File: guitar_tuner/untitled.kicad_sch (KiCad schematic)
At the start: 1 part, among them J1 USB_B_Micro

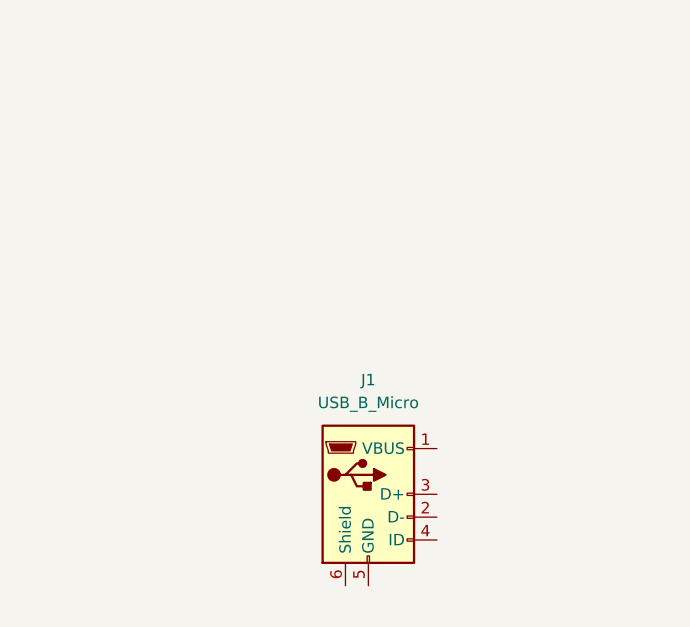
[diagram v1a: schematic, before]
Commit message: Added micro USB B for input power as well as voltage regulator.
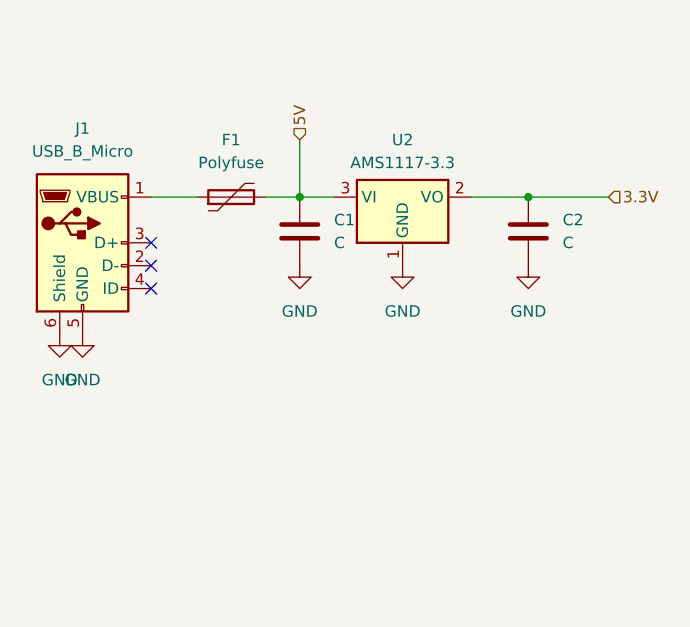
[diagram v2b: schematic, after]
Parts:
- added C1, C2: C, symbol Device:C
- added F1: Polyfuse, symbol Device:Polyfuse
- added U2: AMS1117-3.3, Package_TO_SOT_SMD:SOT-223-3_TabPin2, symbol Regulator_Linear:AMS1117-3.3
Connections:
- net at J1.1 (VBUS): now also F1.1
- net GND: now reaches J1.5 (GND)
- net GND: now also J1.6 (Shield), C1.2, C2.2, U2.1 (GND)
- new net 3.3V: C2.1, U2.2 (VO)
- new net 5V: C1.1, F1.2, U2.3 (VI)
- no-connect marks 0 -> 3

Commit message: Buzzer Circuit
Transistor and buzzer, have not yet set up power or connected to ESP32
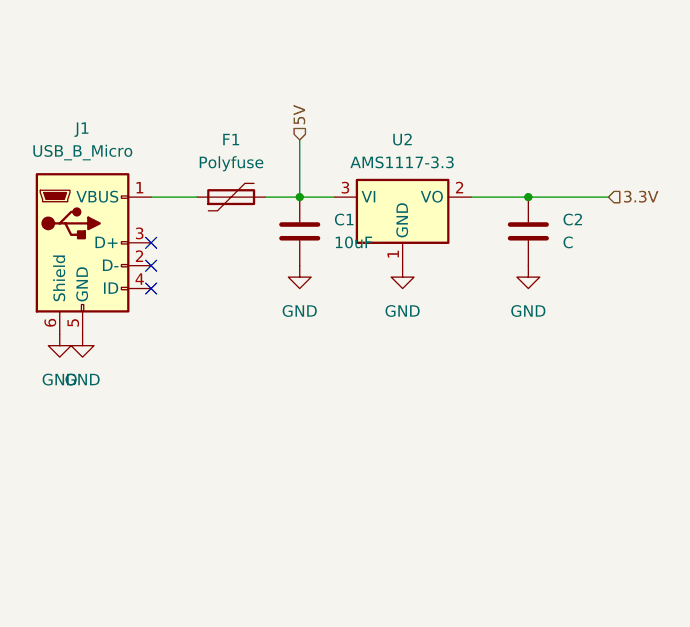
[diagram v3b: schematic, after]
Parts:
- C1: value C -> 10uF
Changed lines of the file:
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@@
 			)
 		)
-		(property "Value" "C"
+		(property "Value" "10uF"
 			(at 85.09 81.2799 0)
 			(effects

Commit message: Connected power to buzzer and audio input circuits, made connections to microcontroller.
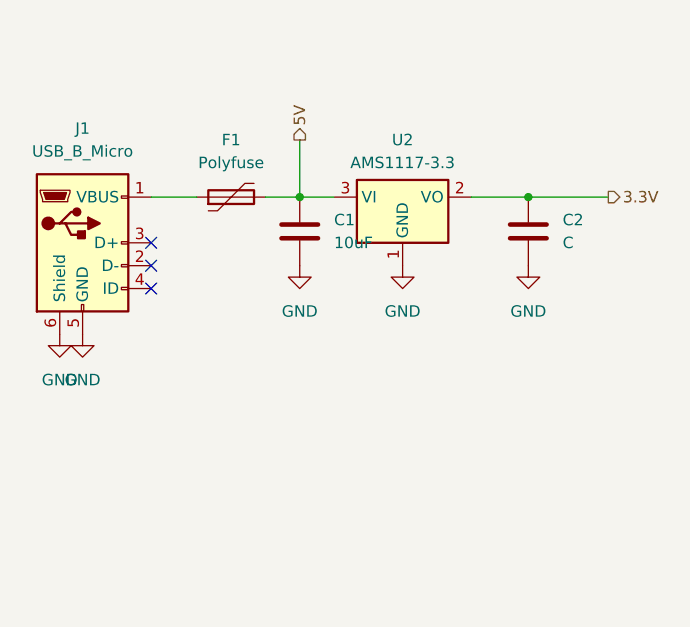
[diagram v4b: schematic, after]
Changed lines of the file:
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@@
 	)
 	(hierarchical_label "5V"
-		(shape input)
+		(shape output)
 		(at 81.28 69.85 90)
 		(effects
@@
 	)
 	(hierarchical_label "3.3V"
-		(shape input)
+		(shape output)
 		(at 115.57 76.2 0)
 		(effects

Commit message: Multiple Schematic Fixes
- Created outputs from the power schematic for the D+ and D- pins and attached them to esp
- Changed net class directives to global labels as net class directives don't properly translate to layout (5V, Audio, 3.3V)
- Fixed buzzer schematic as the esp was not properly connected to it due to mismatched grid sizes
- Added power flags to voltage sources
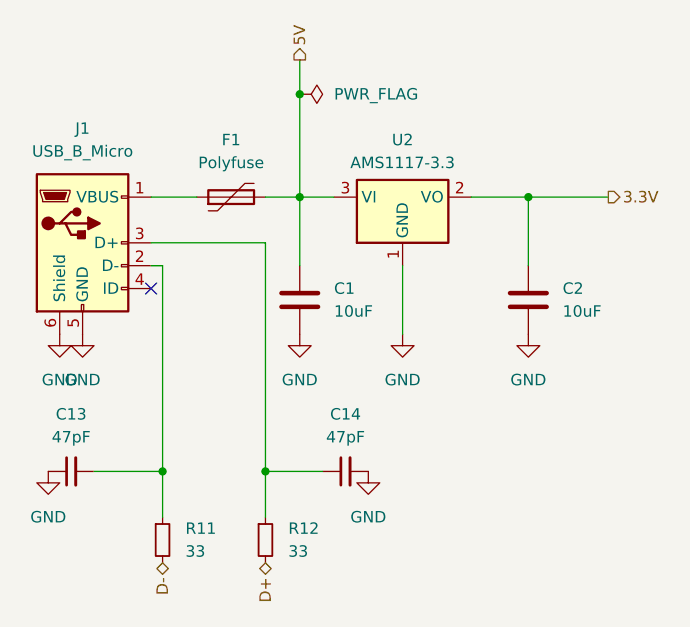
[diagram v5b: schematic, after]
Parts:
- added C13, C14: 47pF, symbol Device:C_Small
- added R11, R12: 33, symbol Device:R_Small
- C2: value C -> 10uF
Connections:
- net GND: now also C13.1, C14.2
- net at J1.2 (D-): now also C13.2, R11.1
- net at J1.3 (D+): now also C14.1, R12.1
- new net D+: R12.2
- new net D-: R11.2
- no-connect marks 3 -> 1
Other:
- moved on the sheet: C1, C2

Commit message: Power Circuit Footprints
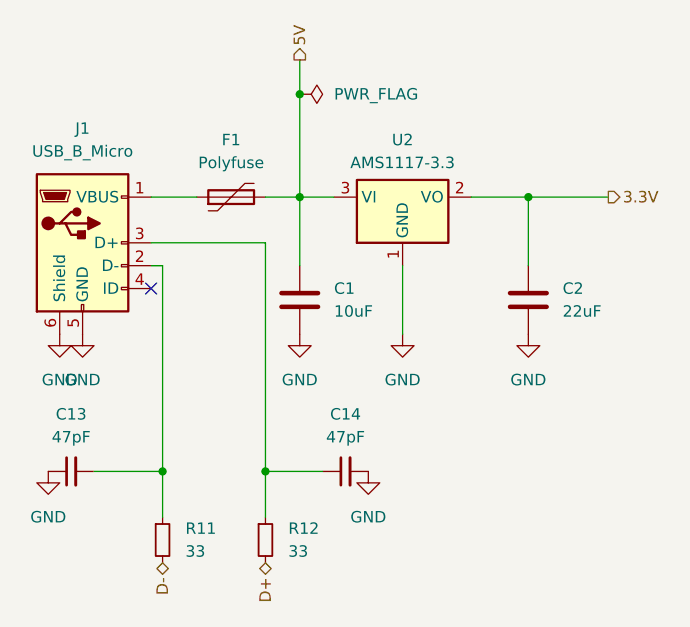
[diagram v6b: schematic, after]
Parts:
- C1, C13, C14: footprint (none) -> Capacitor_SMD:C_0805_2012Metric_Pad1.18x1.45mm_HandSolder
- C2: value 10uF -> 22uF; footprint (none) -> Capacitor_SMD:C_0805_2012Metric_Pad1.18x1.45mm_HandSolder
- F1: footprint (none) -> Fuse:Fuse_0805_2012Metric_Pad1.15x1.40mm_HandSolder
- J1: footprint (none) -> Connector_USB:USB_Micro-B_Wuerth_629105150521
- R11, R12: footprint (none) -> Resistor_SMD:R_0805_2012Metric_Pad1.20x1.40mm_HandSolder
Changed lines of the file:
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@@
 			)
 		)
-		(property "Value" "10uF"
+		(property "Value" "22uF"
 			(at 110.49 88.8999 0)
 			(effects
@@
 			)
 		)
-		(property "Footprint" ""
+		(property "Footprint" "Capacitor_SMD:C_0805_2012Metric_Pad1.18x1.45mm_HandSolder"
 			(at 107.6452 91.44 0)
 			(effects
@@
 			)
 		)
-		(property "Footprint" ""
+		(property "Footprint" "Capacitor_SMD:C_0805_2012Metric_Pad1.18x1.45mm_HandSolder"
 			(at 55.88 106.68 0)
 			(effects
@@
 			)
 		)
-		(property "Footprint" ""
+		(property "Footprint" "Fuse:Fuse_0805_2012Metric_Pad1.15x1.40mm_HandSolder"
 			(at 78.74 74.93 0)
 			(effects
@@
 			)
 		)
-		(property "Footprint" ""
+		(property "Footprint" "Resistor_SMD:R_0805_2012Metric_Pad1.20x1.40mm_HandSolder"
 			(at 66.04 114.3 0)
 			(effects
@@
 			)
 		)
-		(property "Footprint" ""
+		(property "Footprint" "Capacitor_SMD:C_0805_2012Metric_Pad1.18x1.45mm_HandSolder"
 			(at 82.2452 91.44 0)
 			(effects
@@
 			)
 		)
-		(property "Footprint" ""
+		(property "Footprint" "Capacitor_SMD:C_0805_2012Metric_Pad1.18x1.45mm_HandSolder"
 			(at 86.36 106.68 0)
 			(effects
@@
 			)
 		)
-		(property "Footprint" ""
+		(property "Footprint" "Resistor_SMD:R_0805_2012Metric_Pad1.20x1.40mm_HandSolder"
 			(at 77.47 114.3 0)
 			(effects
@@
 			)
 		)
-		(property "Footprint" ""
+		(property "Footprint" "Connector_USB:USB_Micro-B_Wuerth_629105150521"
 			(at 60.96 82.55 0)
 			(effects
